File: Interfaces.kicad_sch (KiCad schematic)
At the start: 9 parts, among them J1 200528-0100, J2 200528-0100, U6 USBLC6-2P6

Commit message: v3.1 Updates
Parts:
- removed C24: 100nF, Capacitor_SMD:C_0603_1608Metric, symbol Device:C_Small
- removed R40, R41, R42, R43: 0R, Resistor_SMD:R_0603_1608Metric, symbol Device:R_Small
- removed U6: USBLC6-2P6, Package_TO_SOT_SMD:SOT-666, symbol Power_Protection:USBLC6-2P6
- added U10: USBLC6-2SC6, Package_TO_SOT_SMD:SOT-23-6, symbol Power_Protection:USBLC6-2SC6
- C43: renamed from C25; value 100nF -> 100n
- J1, J2: value 200528-0100 -> 1-84952-0; footprint Argus-Connectors:Molex_200528-0100_1x10-1MP_P1.00mm_Horizontal -> Connector_FFC-FPC:TE_1-84952-0_1x10-1MP_P1.0mm_Horizontal
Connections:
- net COIL_DRIVER_EN_OR_MAIN_3V3 is gone; now on net COIL_DRIVER_EN: J2.3 (Pin_3)
- net PERI_3V3 is gone; now on net 3V3_P: C43.1
- net PERI_3V3_OR_GND is gone; now on net 3V3_P: J2.5 (Pin_5)
- net GND: now also U10.2 (GND)
- net SCL: now also U10.6 (I/O1)
- net SDA: now also U10.4 (I/O2)
- net SCL_C: now reaches J2.1 (Pin_1)
- net SCL_C: now also U10.1 (I/O1)
- net SDA_C: now reaches J2.2 (Pin_2)
- net SDA_C: now also U10.3 (I/O2)
- net MAIN_3V3 renamed 3V3_P
- net 3V3_P: now also U10.5 (VBUS)
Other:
- company: (none) -> Carnegie Mellon University
- title: (none) -> Argus XY Solar Panel
- moved on the sheet: C43, J1, J2

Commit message: Local Stash
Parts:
- removed U10: USBLC6-2SC6, Package_TO_SOT_SMD:SOT-23-6, symbol Power_Protection:USBLC6-2SC6
- added U11: D5V0P4UR6SO, Package_TO_SOT_SMD:SOT-23-6, symbol Power_Protection:SRV05-4
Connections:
- net SCL_C is gone; now on net SCL: J2.1 (Pin_1)
- net SDA_C is gone; now on net SDA: J2.2 (Pin_2)
- net 3V3_P: now also U11.5 (VP)
- net GND: now also U11.2 (VN)
- net SCL: now also U11.1 (IO1)
- net SDA: now also U11.3 (IO2)
- no-connect marks 0 -> 2
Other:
- moved on the sheet: C43, J1, J2

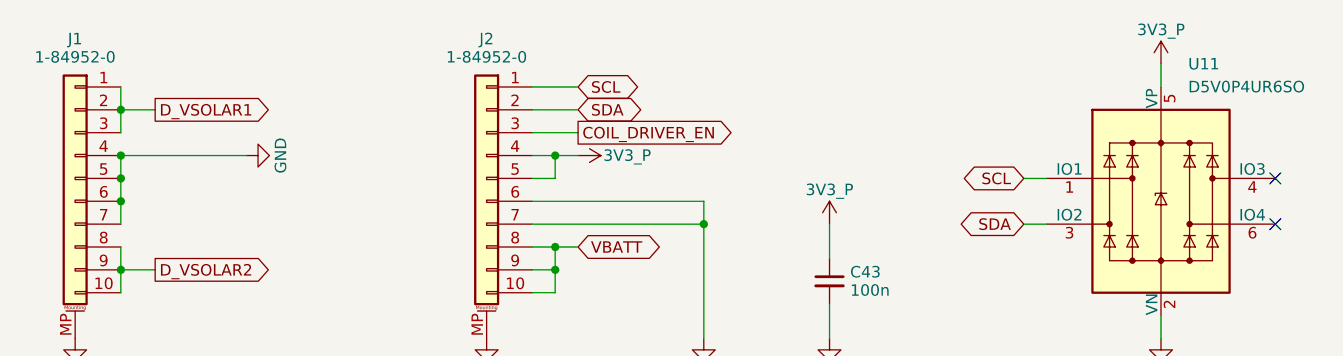
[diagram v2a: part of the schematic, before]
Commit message: Updated access port, added deployment sensor
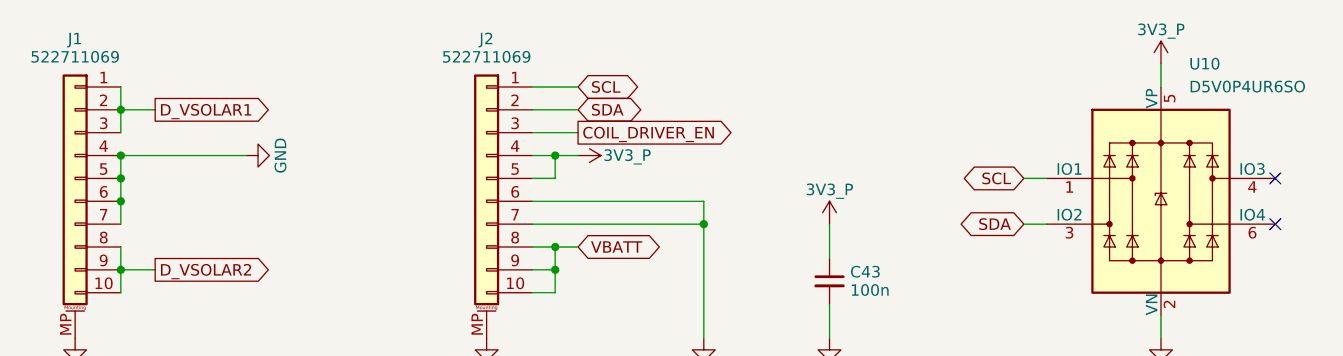
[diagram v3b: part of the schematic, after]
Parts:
- C43: MPN (none) -> C307348
- J1, J2: value 1-84952-0 -> 522711069; footprint Connector_FFC-FPC:TE_1-84952-0_1x10-1MP_P1.0mm_Horizontal -> Argus-Connectors:CON_522711069_MOL; MPN (none) -> C588180
- U10: renamed from U11; MPN (none) -> C531179
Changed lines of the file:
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@@
 			)
 		)
-		(property "Value" "1-84952-0"
+		(property "Value" "522711069"
 			(at 134.62 83.058 0)
 			(effects
@@
 			)
 		)
-		(property "Footprint" "Connector_FFC-FPC:TE_1-84952-0_1x10-1MP_P1.0mm_Horizontal"
+		(property "Footprint" "Argus-Connectors:CON_522711069_MOL"
 			(at 134.62 96.52 0)
 			(effects
@@
 		)
 		(property "Description" "Generic connectable mounting pin connector, single row, 01x10, script generated (kicad-library-utils/schlib/autogen/connector/)"
+			(at 134.62 96.52 0)
+			(effects
+				(font
+					(size 1.27 1.27)
+				)
+				(hide yes)
+			)
+		)
+		(property "MPN" "C588180"
 			(at 134.62 96.52 0)
 			(effects
@@
 			)
 		)
+		(property "MPN" "C307348"
+			(at 172.72 107.95 0)
+			(effects
+				(font
+					(size 1.27 1.27)
+				)
+				(hide yes)
+			)
+		)
 		(pin "1"
 		)
@@
 		(dnp no)
 		(fields_autoplaced yes)
-		(property "Reference" "U11"
-			(at 212.5665 83.82 0)
+		(property "Reference" "U10"
+			(at 212.6681 83.82 0)
 			(effects
 				(font
@@
 		)
 		(property "Value" "D5V0P4UR6SO"
-			(at 212.5665 86.36 0)
+			(at 212.6681 86.36 0)
 			(effects
 				(font
@@
 			)
 		)
+		(property "MPN" "C531179"
+			(at 209.55 99.06 0)
+			(effects
+				(font
+					(size 1.27 1.27)
+				)
+				(hide yes)
+			)
+		)
 		(pin "6"
 		)
@@
 			(project "Avionics-SolarPanels"
 				(path "/92e58b76-9357-4452-b231-18fffdf58e73/281d608c-0adc-47e2-a0e6-d9b27e3edbd5"
-					(reference "U11")
+					(reference "U10")
 					(unit 1)
 				)
@@
 			)
 		)
-		(property "Value" "1-84952-0"
+		(property "Value" "522711069"
 			(at 88.9 83.058 0)
 			(effects
@@
 			)
 		)
-		(property "Footprint" "Connector_FFC-FPC:TE_1-84952-0_1x10-1MP_P1.0mm_Horizontal"
+		(property "Footprint" "Argus-Connectors:CON_522711069_MOL"
 			(at 88.9 96.52 0)
 			(effects
@@
 			(at 88.9 96.52 0)
 			(effects
+				(font
+					(size 1.27 1.27)
+				)
+				(hide yes)
+			)
+		)
+		(property "MPN" "C588180"
+			(at 88.9 96.52 0)
+			(effects
